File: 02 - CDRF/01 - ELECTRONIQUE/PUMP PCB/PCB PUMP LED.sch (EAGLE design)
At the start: 13 parts, among them J3 PWRPAD2-5MM, J4 PWRPAD2-5MM

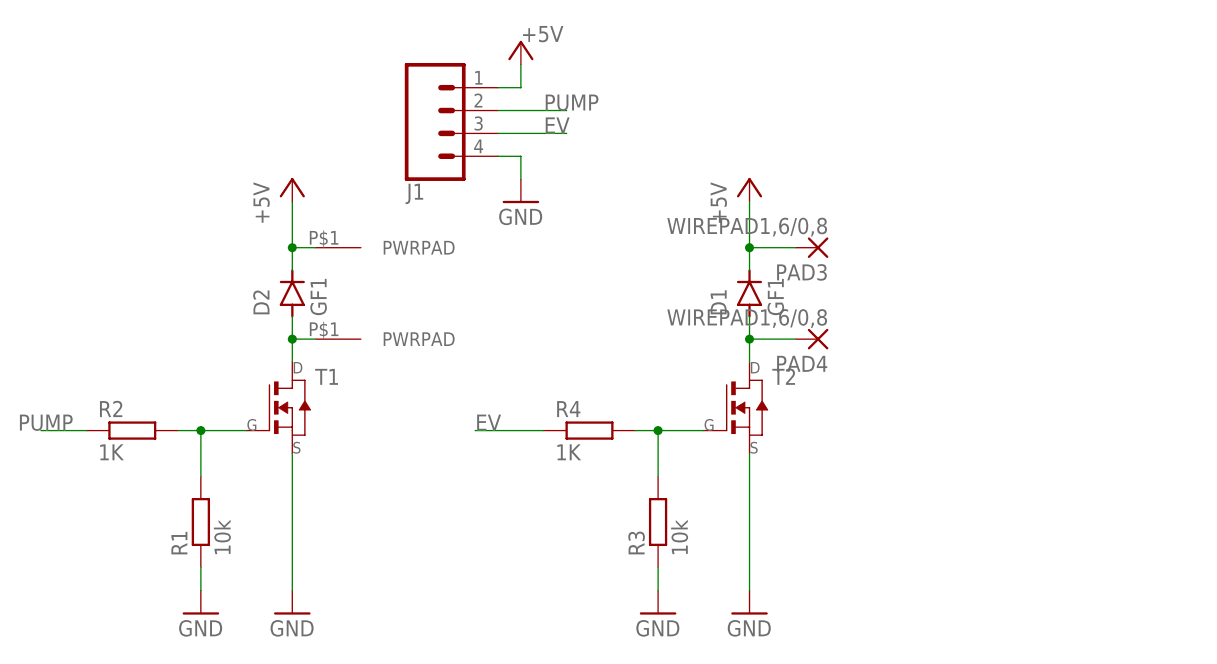
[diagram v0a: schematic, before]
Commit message: update 3D packages
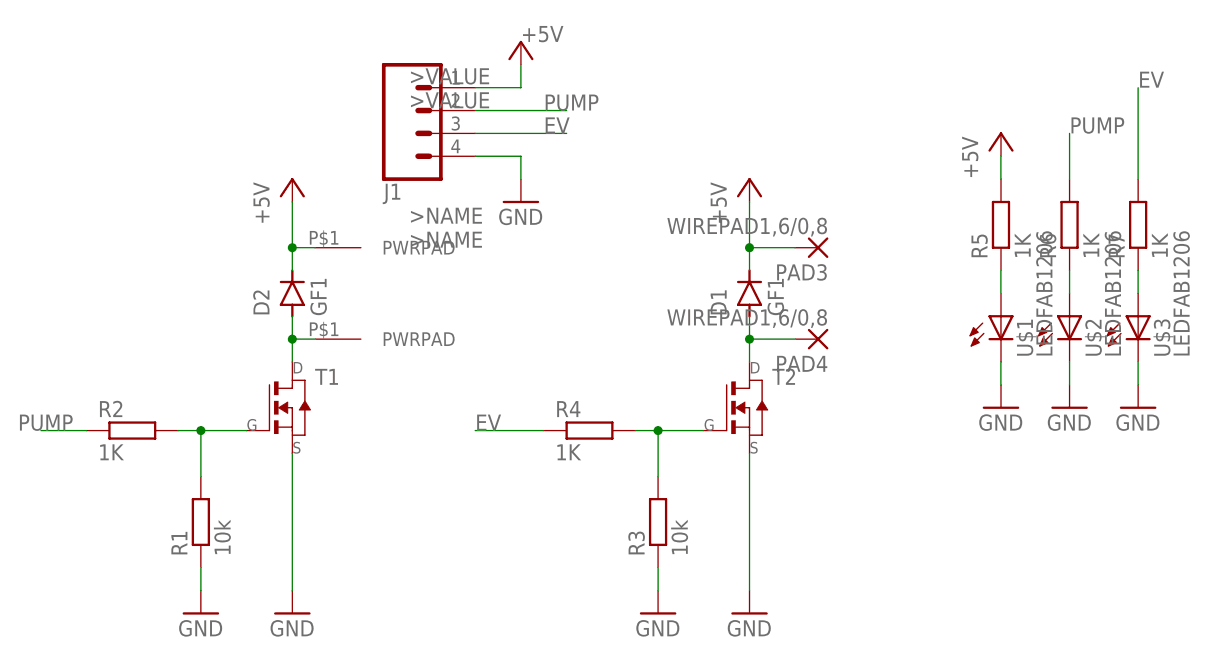
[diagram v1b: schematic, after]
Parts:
- added R5, R6, R7: 1K, rcl:R-EU_R1206
- added U$1, U$2, U$3: LEDFAB1206, fab:LEDFAB1206
- J1: device CONNECTORS:CONN_04POLAR -> OPENBOT:CONN_04POLAR
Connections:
- new net N$5: R5.1, U$1.A
- new net N$6: R6.1, U$2.A
- new net N$7: R7.1, U$3.A
- net +5V: now also R5.2
- net EV: now also R7.2
- net GND: now also U$1.C, U$2.C, U$3.C
- net PUMP: now also R6.2
